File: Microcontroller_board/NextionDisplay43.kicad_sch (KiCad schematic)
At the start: 1 part, among them J6 NextionConnector

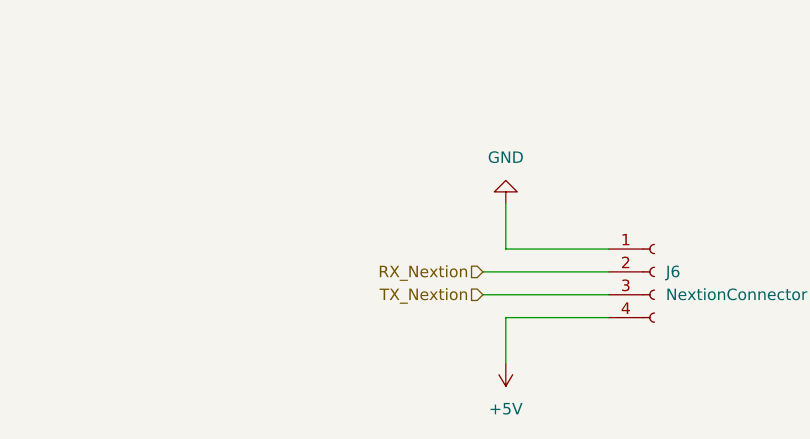
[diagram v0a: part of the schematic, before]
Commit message: Correct the labels for nextion
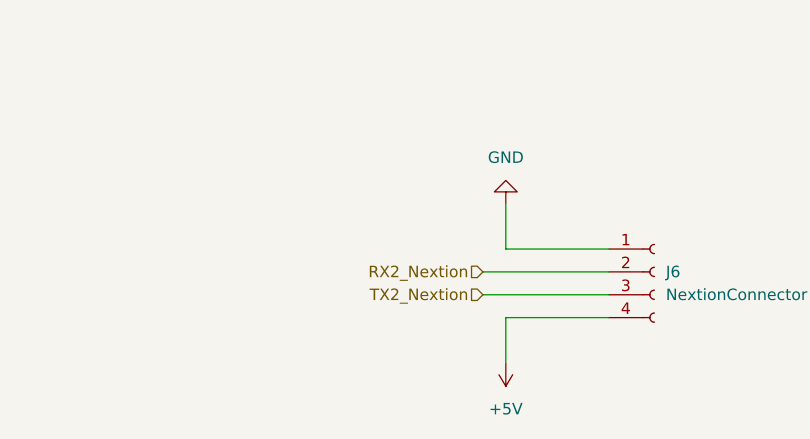
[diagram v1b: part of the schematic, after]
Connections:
- net RX_Nextion renamed RX2_Nextion
- net TX_Nextion renamed TX2_Nextion
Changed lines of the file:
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@@
     (effects (font (size 6 6) (thickness 1.2) bold italic) (justify left bottom))
   )
-  (hierarchical_label "RX_Nextion" (shape input) (at 128.27 86.36 180) (fields_autoplaced)
+  (hierarchical_label "RX2_Nextion" (shape input) (at 128.27 86.36 180) (fields_autoplaced)
     (effects (font (size 1.27 1.27)) (justify right))
   )
-  (hierarchical_label "TX_Nextion" (shape input) (at 128.27 88.9 180) (fields_autoplaced)
+  (hierarchical_label "TX2_Nextion" (shape input) (at 128.27 88.9 180) (fields_autoplaced)
     (effects (font (size 1.27 1.27)) (justify right))
   )
